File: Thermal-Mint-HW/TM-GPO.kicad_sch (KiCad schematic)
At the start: 0 parts

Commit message: Clean up of output circuits
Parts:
- added C32, C33: 470n, Capacitor_SMD:C_0603_1608Metric_Pad1.08x0.95mm_HandSolder, symbol Device:C
- added D1, D2: LED, LED_SMD:LED_0603_1608Metric, symbol Device:LED
- added R33, R34, R35, R36, R37, R38, R39, R40, R41, R42: 1k, Resistor_SMD:R_0603_1608Metric_Pad0.98x0.95mm_HandSolder, symbol Device:R
- added R43: 24, Resistor_SMD:R_0603_1608Metric_Pad0.98x0.95mm_HandSolder, symbol Device:R
- added U6: MAX7317ATE+, Package_DFN_QFN:QFN-16-1EP_3x3mm_P0.5mm_EP1.7x1.7mm, symbol ThermalMint:MAX7317ATE+
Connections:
- new net: D1.1 (K), U6.11 (P9)
- new net: D1.2 (A), R36.1
- new net: D2.1 (K), U6.10 (P8)
- new net: D2.2 (A), R40.1
- new net: R43.1, U6.12 (Dout)
- new net +3V3: C33.1, R36.2, R40.2, U6.14 (V+)
- new net +5V: C32.1, R33.2, R34.2, R35.2, R37.2, R38.2, R39.2, R41.2, R42.2
- new net CS: U6.16 (~{CS})
- new net DIN: U6.13 (DIN)
- new net DOUT: R43.2
- new net GND: C32.2, C33.2, U6.17 (EP), U6.6 (GND)
- new net GPO0: R42.1, U6.1 (P0)
- new net GPO1: R41.1, U6.2 (P1)
- new net GPO2: R39.1, U6.3 (P2)
- new net GPO3: R38.1, U6.4 (P3)
- new net GPO4: R37.1, U6.5 (P4)
- new net GPO5: R35.1, U6.7 (P5)
- new net GPO6: R34.1, U6.8 (P6)
- new net GPO7: R33.1, U6.9 (P7)
- new net SCLK: U6.15 (SCLK)

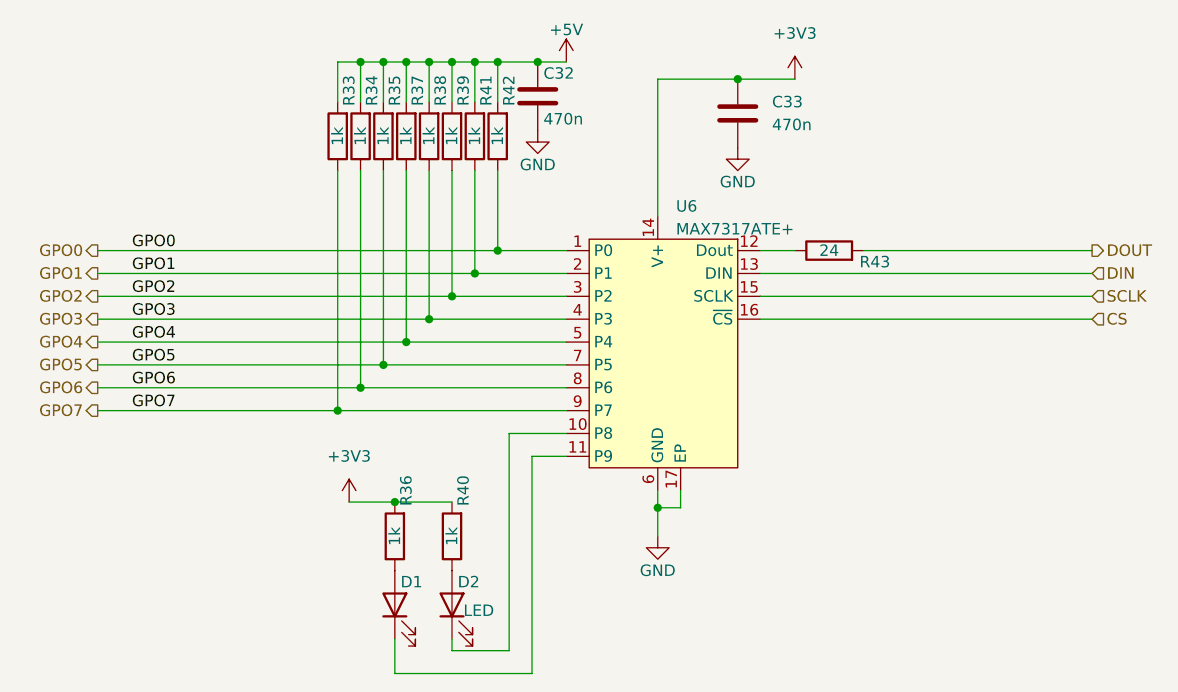
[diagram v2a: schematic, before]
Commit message: Cleanup of Rev1 schematics for review
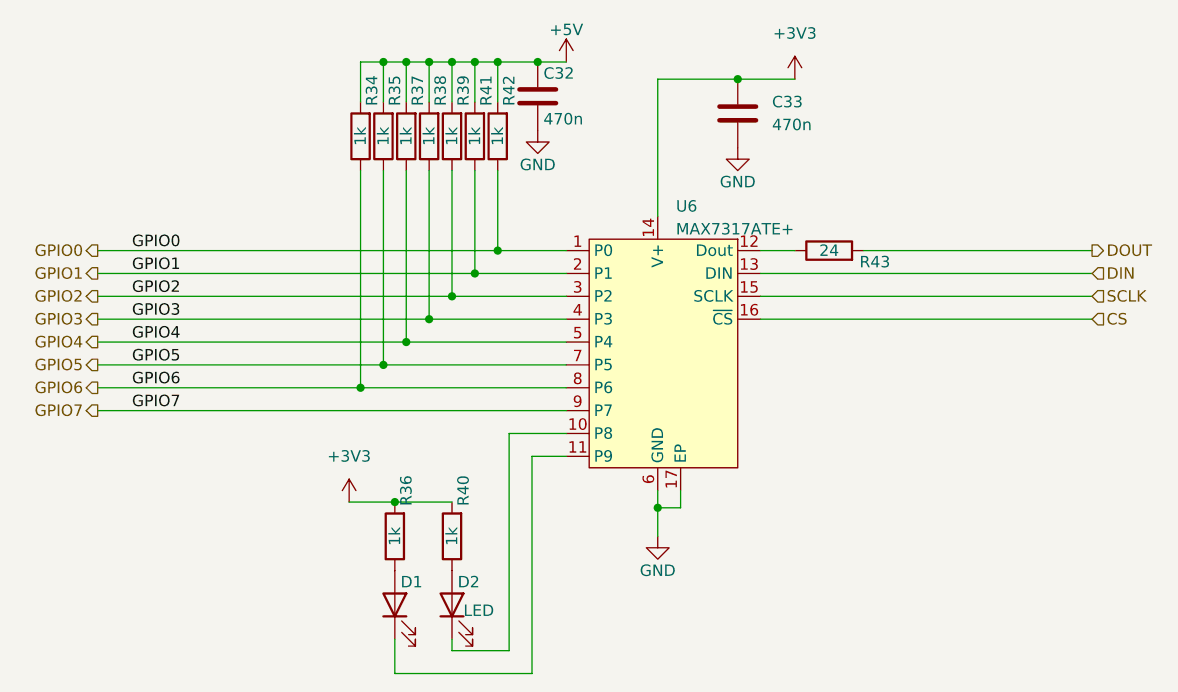
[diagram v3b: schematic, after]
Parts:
- removed R33: 1k, Resistor_SMD:R_0603_1608Metric_Pad0.98x0.95mm_HandSolder, symbol Device:R
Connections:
- net GPO0 renamed GPIO0
- net GPO1 renamed GPIO1
- net GPO2 renamed GPIO2
- net GPO3 renamed GPIO3
- net GPO4 renamed GPIO4
- net GPO5 renamed GPIO5
- net GPO6 renamed GPIO6
- net GPO7 renamed GPIO7
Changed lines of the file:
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@@
   (junction (at 129.54 62.23) (diameter 0) (color 0 0 0 0)
   )
-  (junction (at 124.46 62.23) (diameter 0) (color 0 0 0 0)
-  )
-  (junction (at 121.92 100.965) (diameter 0) (color 0 0 0 0)
-  )
   (junction (at 127 62.23) (diameter 0) (color 0 0 0 0)
   )
@@
     (stroke (width 0) (type default) (color 0 0 0 0))
   )
-  (wire (pts (xy 95.25 100.965) (xy 121.92 100.965))
+  (wire (pts (xy 95.25 100.965) (xy 147.32 100.965))
     (stroke (width 0) (type default) (color 0 0 0 0))
   )
@@
     (stroke (width 0) (type default) (color 0 0 0 0))
   )
-  (wire (pts (xy 121.92 62.23) (xy 124.46 62.23))
-    (stroke (width 0) (type default) (color 0 0 0 0))
-  )
   (wire (pts (xy 168.91 83.185) (xy 172.72 83.185))
     (stroke (width 0) (type solid) (color 0 0 0 0))
@@
     (stroke (width 0) (type default) (color 0 0 0 0))
   )
-  (wire (pts (xy 121.92 74.295) (xy 121.92 100.965))
-    (stroke (width 0) (type default) (color 0 0 0 0))
-  )
   (wire (pts (xy 124.46 98.425) (xy 147.32 98.425))
     (stroke (width 0) (type default) (color 0 0 0 0))
@@
     (stroke (width 0) (type default) (color 0 0 0 0))
   )
-  (wire (pts (xy 121.92 66.675) (xy 121.92 62.23))
-    (stroke (width 0) (type default) (color 0 0 0 0))
-  )
   (wire (pts (xy 160.02 111.76) (xy 160.02 109.855))
     (stroke (width 0) (type default) (color 0 0 0 0))
@@
     (stroke (width 0) (type default) (color 0 0 0 0))
   )
-  (wire (pts (xy 121.92 100.965) (xy 147.32 100.965))
-    (stroke (width 0) (type default) (color 0 0 0 0))
-  )
   (wire (pts (xy 144.145 62.23) (xy 147.32 62.23))
     (stroke (width 0) (type default) (color 0 0 0 0))
@@
     (stroke (width 0) (type solid) (color 0 0 0 0))
   )
-  (label "GPO0" (at 99.06 83.185 0)
-    (effects (font (size 1.27 1.27)) (justify left bottom))
-  )
-  (label "GPO5" (at 99.06 95.885 0)
-    (effects (font (size 1.27 1.27)) (justify left bottom))
-  )
-  (label "GPO7" (at 99.06 100.965 0)
-    (effects (font (size 1.27 1.27)) (justify left bottom))
-  )
-  (label "GPO2" (at 99.06 88.265 0)
-    (effects (font (size 1.27 1.27)) (justify left bottom))
-  )
-  (label "GPO6" (at 99.06 98.425 0)
-    (effects (font (size 1.27 1.27)) (justify left bottom))
-  )
-  (label "GPO4" (at 99.06 93.345 0)
-    (effects (font (size 1.27 1.27)) (justify left bottom))
-  )
-  (label "GPO1" (at 99.06 85.725 0)
-    (effects (font (size 1.27 1.27)) (justify left bottom))
-  )
-  (label "GPO3" (at 99.06 90.805 0)
-    (effects (font (size 1.27 1.27)) (justify left bottom))
-  )
-  (hierarchical_label "GPO2" (shape output) (at 95.25 88.265 180)
+  (label "GPIO0" (at 99.06 83.185 0)
+    (effects (font (size 1.27 1.27)) (justify left bottom))
+  )
+  (label "GPIO5" (at 99.06 95.885 0)
+    (effects (font (size 1.27 1.27)) (justify left bottom))
+  )
+  (label "GPIO7" (at 99.06 100.965 0)
+    (effects (font (size 1.27 1.27)) (justify left bottom))
+  )
+  (label "GPIO2" (at 99.06 88.265 0)
+    (effects (font (size 1.27 1.27)) (justify left bottom))
+  )
+  (label "GPIO6" (at 99.06 98.425 0)
+    (effects (font (size 1.27 1.27)) (justify left bottom))
+  )
+  (label "GPIO4" (at 99.06 93.345 0)
+    (effects (font (size 1.27 1.27)) (justify left bottom))
+  )
+  (label "GPIO1" (at 99.06 85.725 0)
+    (effects (font (size 1.27 1.27)) (justify left bottom))
+  )
+  (label "GPIO3" (at 99.06 90.805 0)
+    (effects (font (size 1.27 1.27)) (justify left bottom))
+  )
+  (hierarchical_label "GPIO2" (shape output) (at 95.25 88.265 180)
     (effects (font (size 1.27 1.27)) (justify right))
   )
@@
     (effects (font (size 1.27 1.27)) (justify left))
   )
-  (hierarchical_label "GPO4" (shape output) (at 95.25 93.345 180)
-    (effects (font (size 1.27 1.27)) (justify right))
-  )
-  (hierarchical_label "GPO0" (shape output) (at 95.25 83.185 180)
+  (hierarchical_label "GPIO4" (shape output) (at 95.25 93.345 180)
+    (effects (font (size 1.27 1.27)) (justify right))
+  )
+  (hierarchical_label "GPIO0" (shape output) (at 95.25 83.185 180)
     (effects (font (size 1.27 1.27)) (justify right))
   )
@@
     (effects (font (size 1.27 1.27)) (justify left))
   )
-  (hierarchical_label "GPO6" (shape output) (at 95.25 98.425 180)
+  (hierarchical_label "GPIO6" (shape output) (at 95.25 98.425 180)
     (effects (font (size 1.27 1.27)) (justify right))
   )
@@
     (effects (font (size 1.27 1.27)) (justify left))
   )
-  (hierarchical_label "GPO5" (shape output) (at 95.25 95.885 180)
-    (effects (font (size 1.27 1.27)) (justify right))
-  )
-  (hierarchical_label "GPO3" (shape output) (at 95.25 90.805 180)
-    (effects (font (size 1.27 1.27)) (justify right))
-  )
-  (hierarchical_label "GPO1" (shape output) (at 95.25 85.725 180)
+  (hierarchical_label "GPIO5" (shape output) (at 95.25 95.885 180)
+    (effects (font (size 1.27 1.27)) (justify right))
+  )
+  (hierarchical_label "GPIO3" (shape output) (at 95.25 90.805 180)
+    (effects (font (size 1.27 1.27)) (justify right))
+  )
+  (hierarchical_label "GPIO1" (shape output) (at 95.25 85.725 180)
     (effects (font (size 1.27 1.27)) (justify right))
   )
@@
     (effects (font (size 1.27 1.27)) (justify left))
   )
-  (hierarchical_label "GPO7" (shape output) (at 95.25 100.965 180)
+  (hierarchical_label "GPIO7" (shape output) (at 95.25 100.965 180)
     (effects (font (size 1.27 1.27)) (justify right))
   )
@@
       (effects (font (size 1.27 1.27)) hide)
     )
-    (pin "1")
-    (pin "2")
-  )
-  (symbol (lib_id "Device:R") (at 121.92 70.485 180) (unit 1)
-    (in_bom yes) (on_board yes)
-    (property "Reference" "R33" (id 0) (at 123.19 65.405 90))
-    (property "Value" "1k" (id 1) (at 121.92 70.485 90))
-    (property "Footprint" "Resistor_SMD:R_0603_1608Metric_Pad0.98x0.95mm_HandSolder" (id 2) (at 123.698 70.485 90)
-      (effects (font (size 1.27 1.27)) hide)
-    )
-    (property "Datasheet" "~" (id 3) (at 121.92 70.485 0)
-      (effects (font (size 1.27 1.27)) hide)
-    )
